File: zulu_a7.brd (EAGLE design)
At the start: 61 x 25.4 mm, 183 parts, among them J1 Pmod 2x6, Q1 12MHz 25ppm (FPGA + FT2232HQ), Q3 MBT3904DW1T1, U1 XC7A35T-1CPG236C, U10 93LC46BT-I/SN, U2 FT2232HQ USB-UART/JTAG Bridge, U3 AS4C32M16SB-6TIN, U4 W25Q128JVSIQ, U8 LTC3569EUDC#TRPBF, X1 Molex 105017-0001 Micro-USB-B

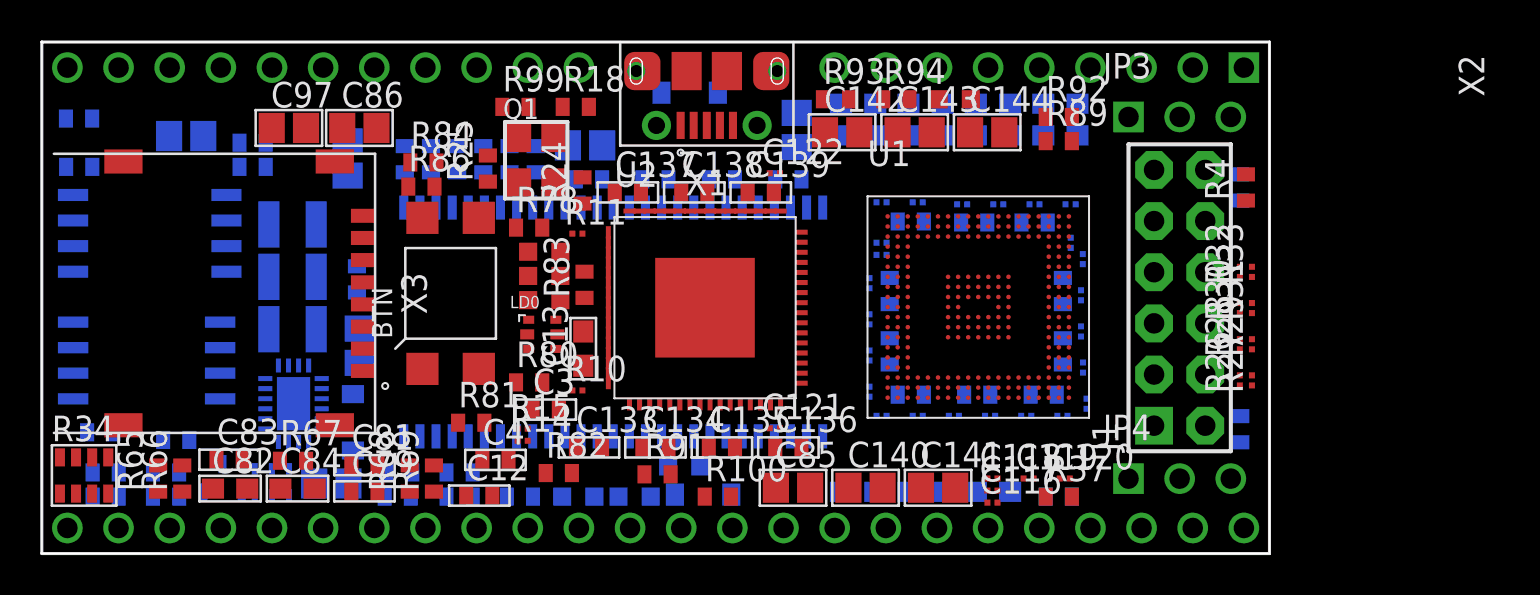
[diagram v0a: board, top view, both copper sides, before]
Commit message: U2's support drops to 0201 where the physics allows: 24 of 36
Fifteen resistors and nine capacitors on the FT2232's sheet.

THE RESISTORS ARE NOT CLOSE TO ANY LIMIT. Every one converted is a pull-up,
pull-down or high-value series: the ten 10k at 1.1 mW, R99 at 2.3, R5 at 2.1,
R101 at 4.9, R24/R25 carrying AC only at about 1.3. Against an 0201's 50 mW
that is 2 to 10 percent. R5 was the last 0603 on the sheet and is now 0201 with
it; it also loses a non-Yageo part number for the same series as its siblings.

THE CAPACITORS ARE THE POINT, THOUGH. 0.1 uF is the value where 0201 actually
works -- bias derating at 0.1 uF is mild, which is exactly what it is not at the
0.47 uF on sheet 7. And C40 and C41 sit on FT-VPHY and FT-VPLL, the USB PHY and
PLL supplies, where lower ESL is worth having rather than merely tolerable.

But the dielectric changes and that is recorded on every one: X7R 16V becomes
X5R 10V, because 0201 at this capacitance is an X5R part. X5R stops at +85 C
where X7R goes to +125. Fine for this board, not a like-for-like swap. C38 drops
50V to 25V, which was over-specified for a 3.3V rail either way.

TWO DID NOT MOVE AND BOTH SAY WHY ON THE PART.
  R100  330R holding DONE low through configuration is 33 mW: 53 percent of an
        0402 but 66 of an 0201, sustained for all of config and indefinitely if
        config fails. 330R on DONE is standard Xilinx practice, so the value is
        not the thing to change -- the package is where the margin is.
  R18   the FT2232's RREF, which sets USB transceiver bias. 0.9 mW and 1 percent
        is 1 percent at any size, but there is no space pressure left on this
        board, so there is nothing to win against a part whose drift shows up as
        signal quality.

The six 100R JTAG series stay 0402 for the reason already recorded when R4 was
split, and C39/C139 stay because 3.3 uF does not exist in 0201.

CHECK_BOARD CAUGHT A BUG VALIDATE DID NOT. All nine capacitors are on C-GENERIC,
not C-US, and C-GENER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
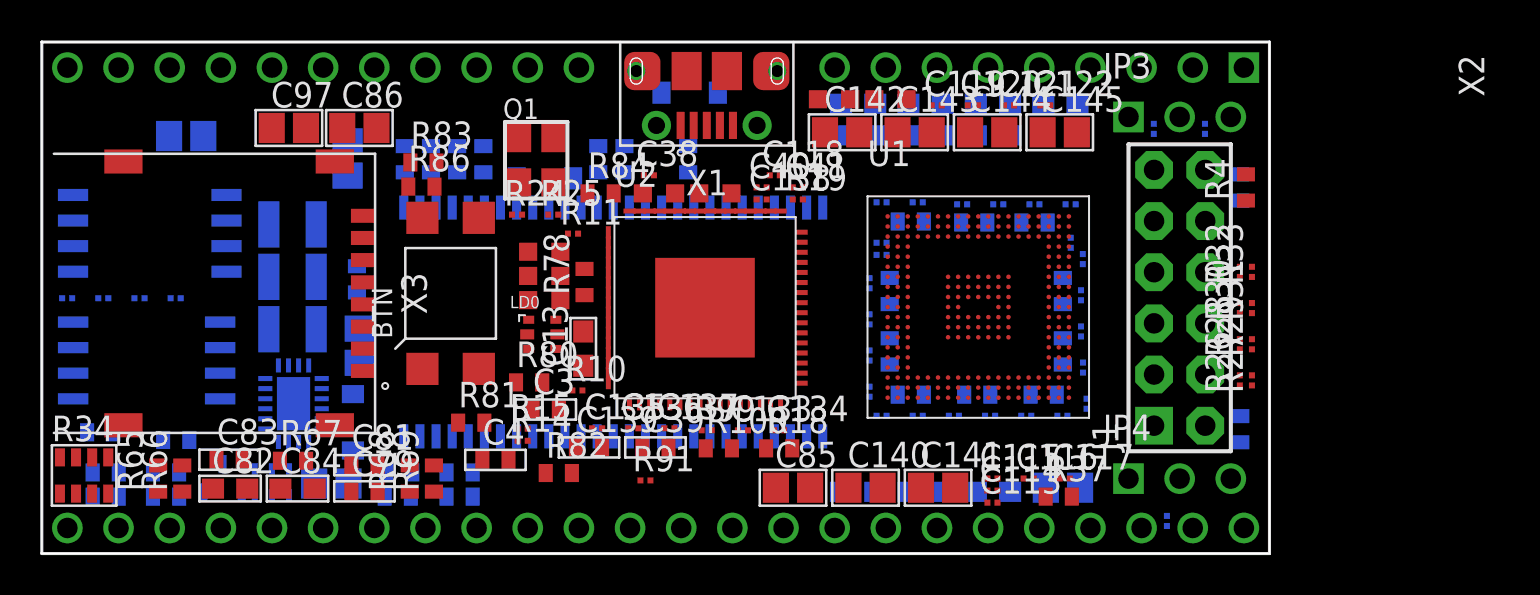
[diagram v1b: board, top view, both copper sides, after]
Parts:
- C133, C134, C135, C136, C137, C138, C38, C40, C41: device rcl:C0402 -> rcl:C0201
- R101, R19, R24, R25, R89, R90, R91, R92, R93, R94, R96, R97, R98, R99: device rcl:R0402 -> rcl:R0201
- R5: device rcl:R0603 -> rcl:R0201
- moved C146 29.2 mm to (50.7, 3.27)
- moved L7 20.9 mm to (42.1, 22.6), flipped to the top
- moved R19 20.2 mm to (37.5, 17.6), flipped to the top
- moved C121 19.8 mm to (48.0, 22.3)
- moved R18 19.7 mm to (36.6, 5.22)
- moved C12 19.7 mm to (32.1, 19.6), flipped to the bottom, turned to 90 degrees
- moved C119 19.1 mm to (44.4, 22.3)
- moved C120 19.1 mm to (46.2, 22.3)
- moved R99 18.7 mm to (33.0, 6.12)
- moved C118 18.5 mm to (36.4, 18.8)
- moved D3 17.6 mm to (25.0, 18.6)
- moved L4 15.6 mm to (30.6, 17.9), flipped to the top
- moved L5 15.6 mm to (33.4, 17.9), flipped to the top
- moved C139 15.3 mm to (27.2, 5.27)
- moved C122 13.8 mm to (49.8, 22.3)
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
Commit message: Regenerate the board: four element values had not reached it
I said several times that attribute-only edits do not need the board rebuilt.
That is true of MANF, MANF# and SPEC, which live only in the schematic. It is
NOT true of value: an EAGLE element carries its own value string, so LD1 and LD2
still read "LED" on the board, and LD5 and Q2 read empty, while the schematic
had red, red, green and 2N7002.

check_board did not catch it and is not wrong to have missed it -- it compares
parts to elements by package and nets to signals by contactref, which is what
consistency means for connectivity. A value is a label. It is also what gets
silkscreened and what a pick-and-place file carries, so it is worth having right.

Regenerated: 178 placed, 0 real parts parked, check_board 0 findings, and no
element value now differs from its part.

Co-Authored-By: Claude Opus 5 <noreply@anthropic.com>
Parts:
- LD1, LD2: value LED -> red
- LD5: value (none) -> green
- Q2: value (none) -> 2N7002
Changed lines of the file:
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@@
 <element name="R77" library="rcl" package="R0402" value="100K" x="20.744" y="4.028" rot="MR0"/>
 <element name="R78" library="rcl" package="R0402" value="680" x="26.95" y="13.483" rot="R90"/>
-<element name="LD5" library="ctambe" package="LED0603" value="" x="24.95" y="14.985"/>
-<element name="Q2" library="ctambe" package="SOT23-3" value="" x="8.975" y="3.74" rot="MR0"/>
+<element name="LD5" library="ctambe" package="LED0603" value="green" x="24.95" y="14.985"/>
+<element name="Q2" library="ctambe" package="SOT23-3" value="2N7002" x="8.975" y="3.74" rot="MR0"/>
 <element name="X1" library="ctambe" package="MOLEX-105017-0001" value="Molex 105017-0001 Micro-USB-B" x="33.02" y="21.259"/>
 <element name="R80" library="rcl" package="R0402" value="182" x="24.198" y="8.4975"/>
@@
 <element name="R94" library="rcl" package="R0201" value="10K" x="49.29" y="17.34" rot="MR0"/>
 <element name="LD0" library="ctambe" package="VS-NRD8" value="VS NRD8" x="24.85" y="10.885"/>
-<element name="LD1" library="ctambe" package="LED0603" value="LED" x="24.95" y="12.585"/>
-<element name="LD2" library="ctambe" package="LED0603" value="LED" x="24.95" y="13.785"/>
+<element name="LD1" library="ctambe" package="LED0603" value="red" x="24.95" y="12.585"/>
+<element name="LD2" library="ctambe" package="LED0603" value="red" x="24.95" y="13.785"/>
 <element name="BTN" library="ctambe" package="PTA-142" value="PTA-142" x="20.3" y="12.92" rot="R90"/>
 <element name="Q1" library="ctambe" package="32X25" value="12MHz 25ppm (FPGA + FT2232HQ)" x="23.7" y="20.63"/>

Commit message: Balance the RGB LED, and correct what I said was wrong with it
FIRST, THE RETRACTION. I said green and blue had "no headroom" and their current
was "set by the diode knee", implying they might barely light. That was wrong,
and the error was mine: I took Vf = 3.3 V typical from the datasheet's 20 mA
table and applied it at a 2 mA operating point. The datasheet's own Vf/If curve
on page 3 puts Vf near 3.0 V down there. Worked properly, the circuit as built
gives red 6.9 mA, green 1.9 and blue 1.5. All three light.

Cmod A7 ships the identical circuit -- same VS NRD8, same 182/182/100 off 3V3,
per its schematic in Datasheet/cmod_a7_sch.pdf. Zulu A7 inherited it whole.

WHAT IS ACTUALLY WRONG IS BALANCE, NOT HEADROOM. Red is an AlGaInP die at about
1.9 V with real margin on a 3.3 V rail; green and blue are 3.3 V-class dice with
almost none. So red ran at four times either of them and dominated every colour
the three are mixed into. Headroom itself cannot be fixed with resistors -- that
is the rail against the die -- but the imbalance can:

    R81 red    182 -> 330    6.9 mA -> 3.8
    R82 green  100 ->  33    1.9 mA -> 2.9
    R80 blue   182 ->  33    1.5 mA -> 2.9

Both new values are already on this board, so the BOM gains no line -- and the
182 ohm line disappears entirely, since R80 and R81 were the only two.

THE TRADE IS REAL AND WORTH STATING. A smaller resistor makes green's current
MORE sensitive in percentage terms: a part 0.15 V high in Vf keeps 77 percent of
nominal at 100R but only 61 at 33R. The absolute floor is what an eye sees,
though, and that rises -- 1.4 mA to 1.8. Nominal and worst case both improve.

LD0's note is rewritten to say this correctly rather than to warn about a
failure that was not there.

178 placed, check_board and validate 0 findings. Regenerated, because element
values changed.

Co-Authored-By: Claude Opus 5 <noreply@anthropic.com>
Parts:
- R80: value 182 -> 33
- R81: value 182 -> 330
- R82: value 100 -> 33
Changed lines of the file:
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@@
 <element name="Q2" library="ctambe" package="SOT23-3" value="2N7002" x="8.975" y="3.74" rot="MR0"/>
 <element name="X1" library="ctambe" package="MOLEX-105017-0001" value="Molex 105017-0001 Micro-USB-B" x="33.02" y="21.259"/>
-<element name="R80" library="rcl" package="R0402" value="182" x="24.198" y="8.4975"/>
-<element name="R81" library="rcl" package="R0402" value="182" x="21.323" y="6.4975"/>
-<element name="R82" library="rcl" package="R0402" value="100" x="25.673" y="3.9975"/>
+<element name="R80" library="rcl" package="R0402" value="33" x="24.198" y="8.4975"/>
+<element name="R81" library="rcl" package="R0402" value="330" x="21.323" y="6.4975"/>
+<element name="R82" library="rcl" package="R0402" value="33" x="25.673" y="3.9975"/>
 <element name="R83" library="rcl" package="R0402" value="330" x="18.948" y="19.42"/>
 <element name="R84" library="rcl" package="R0402" value="330" x="27.748" y="17.883"/>

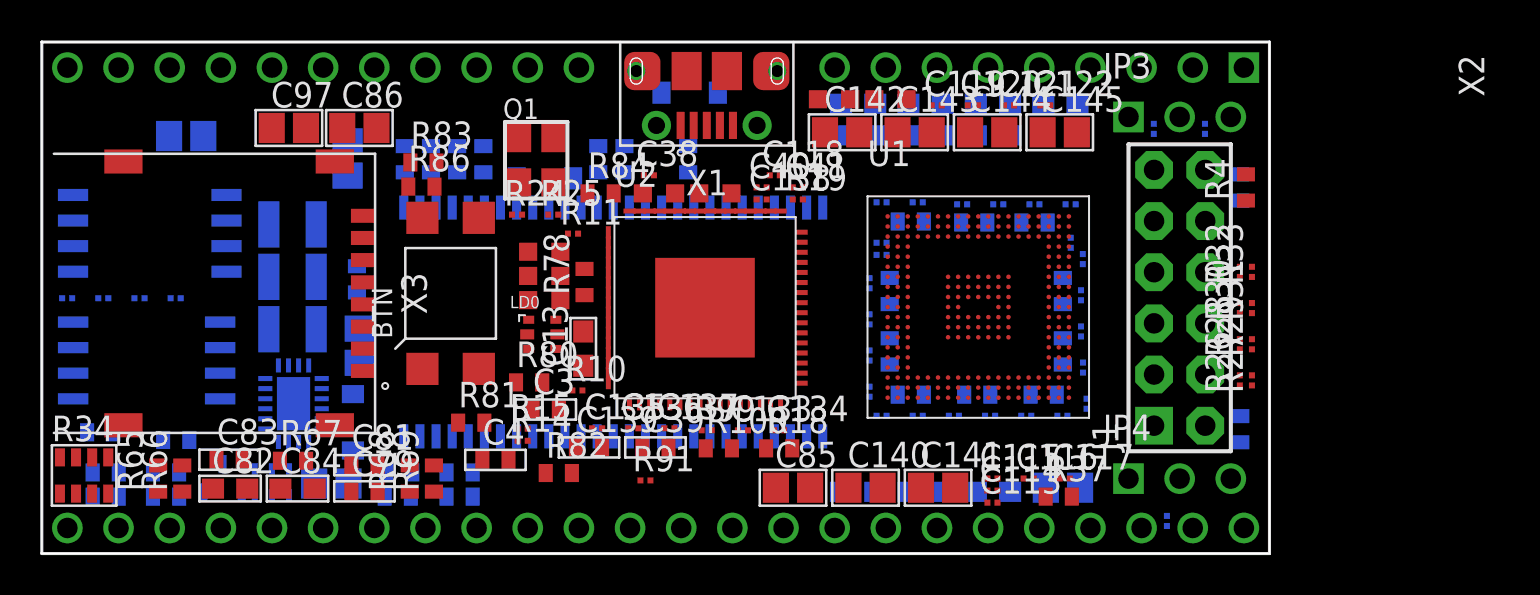
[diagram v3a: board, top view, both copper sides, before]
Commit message: Fix the 0201 land: the heel was positive, which is how 0201 tombstones
The land I drew was pads 0.30 x 0.30 on a 0.20 gap. Measured against the
standardised 0201 body -- 0.60 x 0.30 with 0.15 mm terminals -- that is toe
+0.10, HEEL +0.05, side 0.00.

The heel is the defect. A positive heel puts 0.05 mm of pad under the body at
each end, and solder wicking in under one end before the other wets is the
classic 0201 tombstone mechanism. IPC puts heel at 0.00 for chips this size and
spends the margin on the toe instead, where the fillet is also the one an
inspector can actually see.

Pads move out to +-0.30: gap 0.30, span 0.90, toe +0.15, heel 0.00, side 0.00.
The keepout follows, 1.746 -> 1.846, keeping the same absolute margin past
copper that R0402 uses -- +0.473 in x, which is room for a fan-out via and does
not shrink just because the part did.

Both R0201 and C0201, which stay identical to each other, the way R0402 and
C0402 already are.

The description now carries the derivation instead of the word PROVISIONAL: body
dimensions, the three fillets, and why this is NOT scaled from R0402, whose
0.50 mm toe and 0.20 side suit hand work at 0402 and cause exactly the
tombstoning above at 0201.

WHAT IS STILL NOT VERIFIED, AND CANNOT BE FROM HERE. There is no passive
datasheet and no footprint library on this machine, so no maker's recommended
land was available to check against -- the geometry above is derived from the
component dimensions and standard fillet practice, not copied from a source.
0201 land geometry also belongs to the assembler's process as much as to the
part. The description says so and the caveat stays.

Regenerated: 178 placed, 0 real parts parked, check_board and validate 0
findings, and the wider land did not displace anything.

Co-Authored-By: Claude Opus 5 <noreply@anthropic.com>
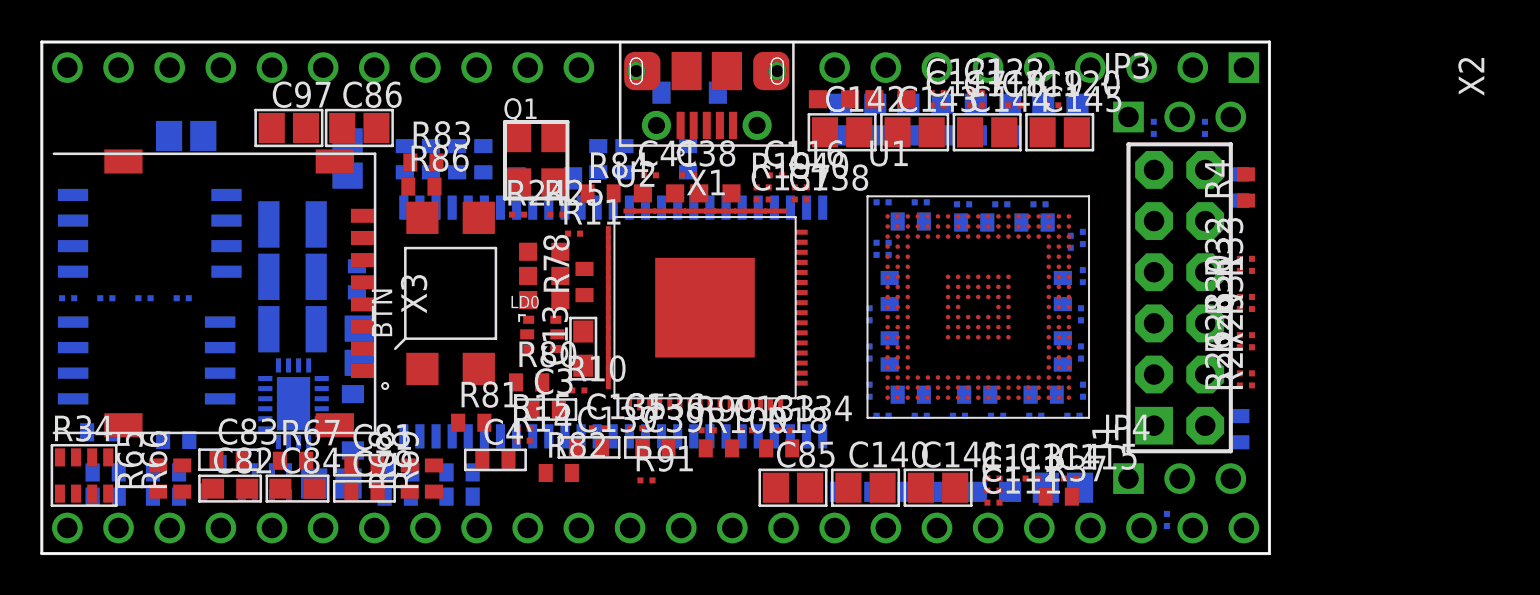
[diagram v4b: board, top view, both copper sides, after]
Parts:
- moved C116 19.6 mm to (36.4, 18.8)
- moved C117 19.6 mm to (44.5, 22.3)
- moved C111 12.5 mm to (47.3, 2.53), flipped to the top, turned to 0 degrees
- moved C112 12.3 mm to (47.3, 3.13), flipped to the top, turned to 0 degrees
- moved C137 12.3 mm to (35.8, 17.6)
- moved C109 10.8 mm to (51.7, 13.8)
- moved C118 10.6 mm to (46.4, 22.3)
- moved C91 9.65 mm to (41.1, 8.09), turned to 90 degrees
- moved C89 9.34 mm to (41.7, 17.4)
- moved C41 7.37 mm to (30.2, 18.8)
- moved C120 3.94 mm to (50.2, 22.3)
- moved C115 3.84 mm to (51.0, 3.73)
- moved C119 3.84 mm to (48.3, 22.3)
- moved C121 3.59 mm to (44.5, 22.9)
- moved C122 3.49 mm to (46.4, 22.9)
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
